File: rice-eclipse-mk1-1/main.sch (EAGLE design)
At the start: 197 parts, among them IC1 LMV321LICTRT, IC10 MCP6N11R, IC11 MCP6N11R, IC12 MCP6N11R, IC13 LMV321LICTRT, IC14 LMV321LICTRT, IC15 LMV321LICTRT, IC16 LMV321LICTRT, IC17 LMV321LICTRT, IC2 LMV321LICTRT, IC3 LMV321LICTRT, IC4 LMV321LICTRT, IC5 MCP6N11R, IC6 LMV321LICTRT, IC7 LMV321LICTRT, IC8 LMV321LICTRT, IC9 LMV321LICTRT, U6 1101M2S3CQE2

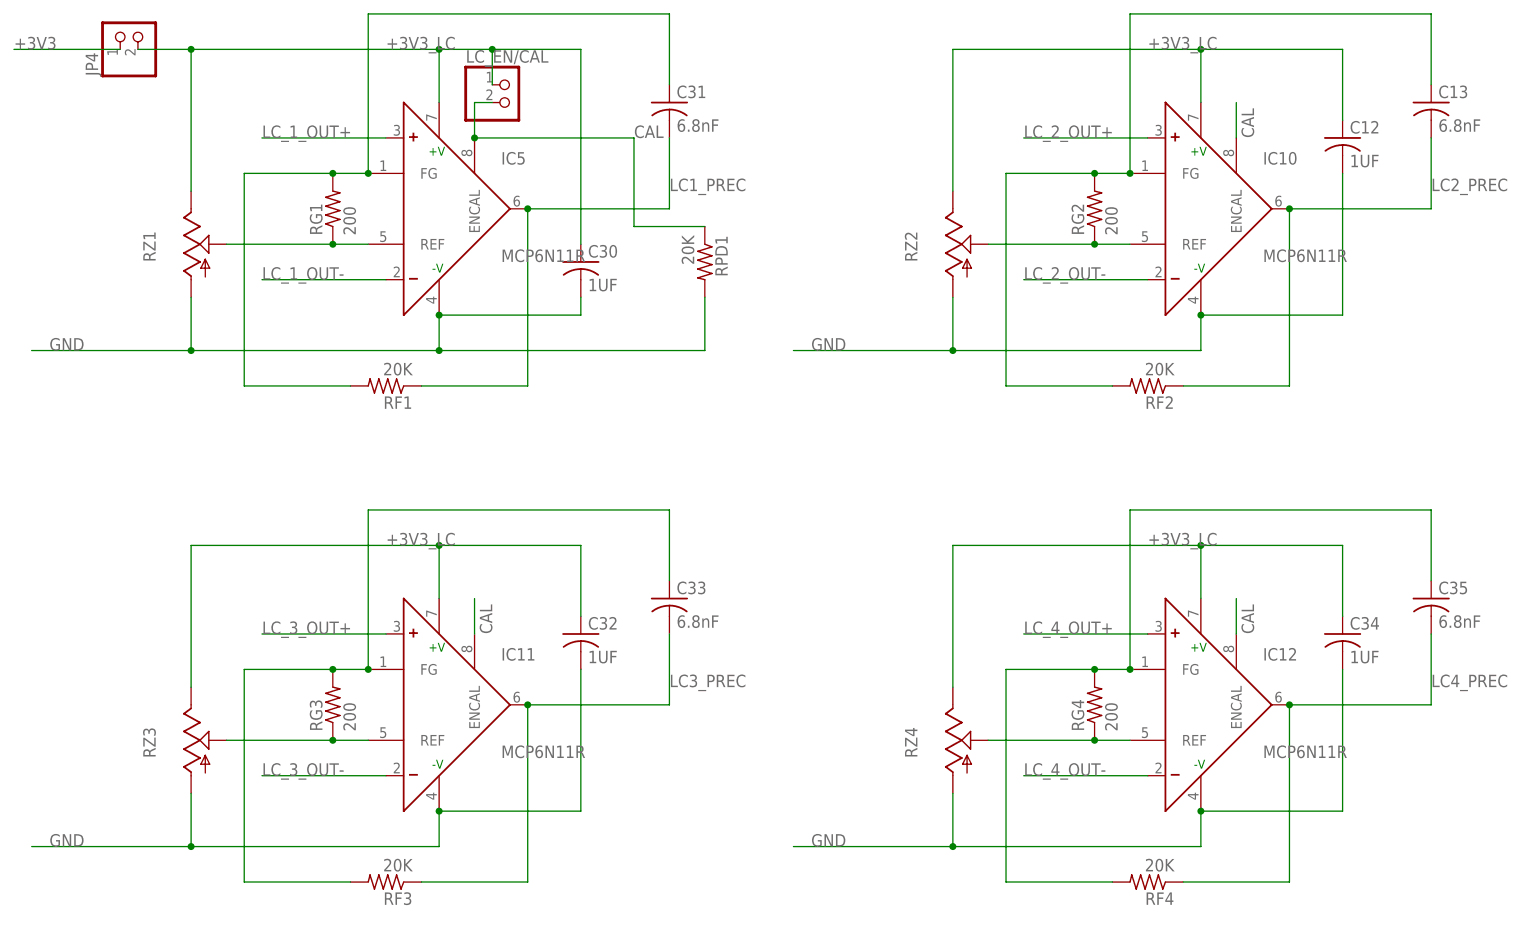
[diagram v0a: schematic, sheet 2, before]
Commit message: New schematics for Titan amp
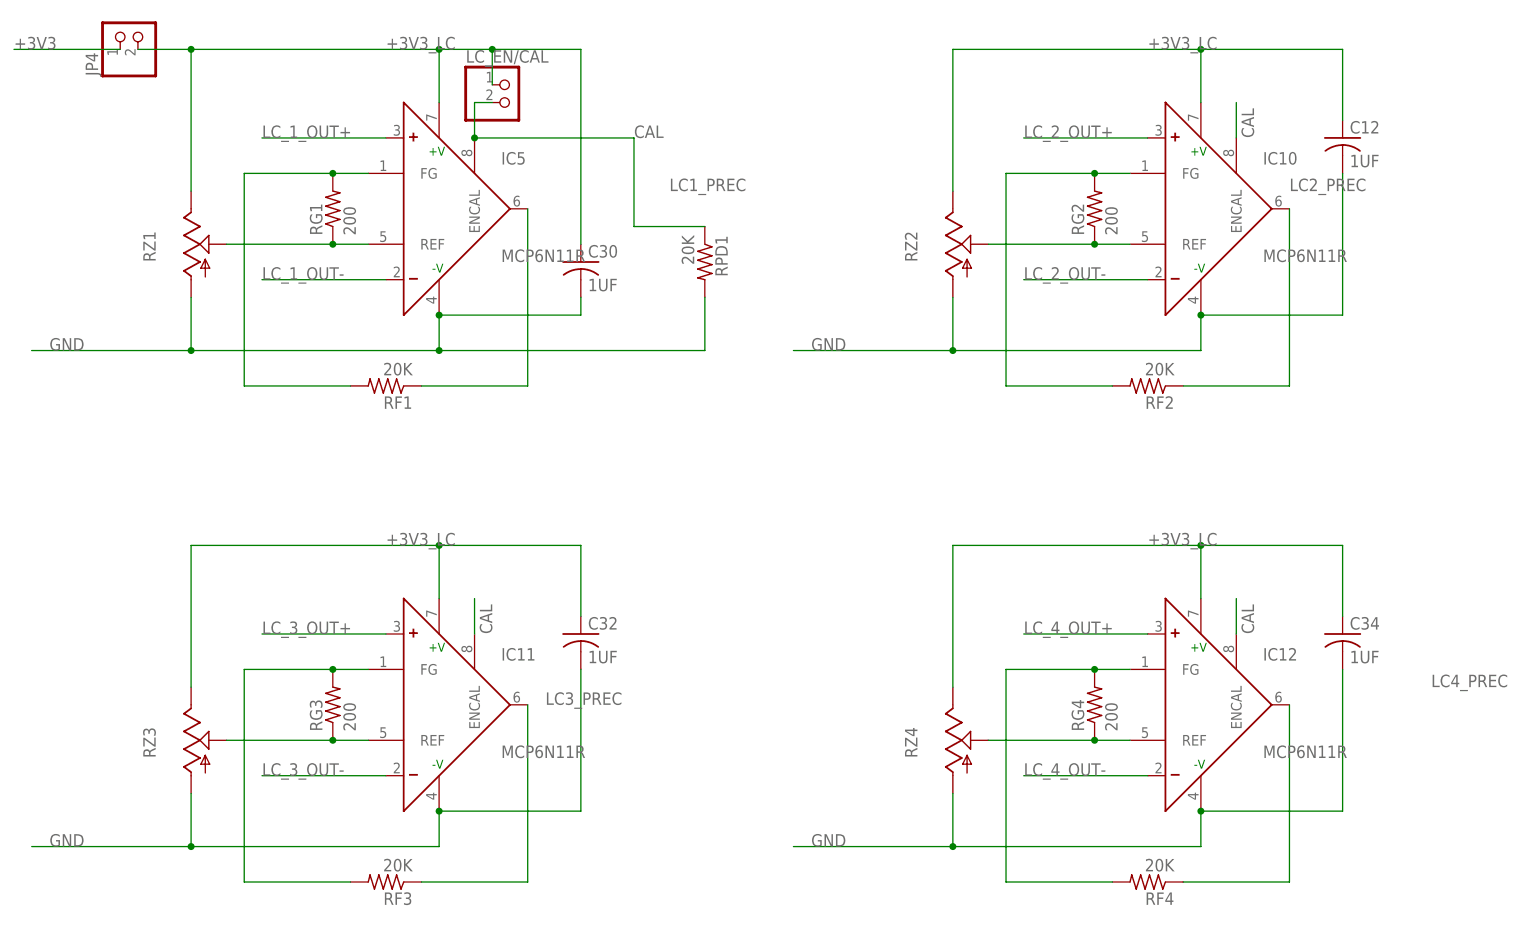
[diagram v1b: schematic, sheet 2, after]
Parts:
- removed C13, C31, C33, C35: 6.8nF, rcl:C-USC0805
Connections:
- net LC1_PREC: no longer C31.2
- net LC2_PREC: no longer C13.2
- net LC3_PREC: no longer C33.2
- net LC4_PREC: no longer C35.2
- net N$21: no longer C13.1
- net N$39: no longer C33.1
- net N$41: no longer C31.1
- net N$46: no longer C35.1
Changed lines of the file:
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@@
 <?xml version="1.0" encoding="utf-8"?>
 <!DOCTYPE eagle SYSTEM "eagle.dtd">
-<eagle version="8.7.1">
+<eagle version="8.7.0">
 <drawing>
 <settings>
-<setting alwaysvectorfont="yes"/>
+<setting alwaysvectorfont="no"/>
 <setting keepoldvectorfont="yes"/>
 <setting verticaltext="up"/>
@@
 <part name="C30" library="rcl" library_urn="urn:adsk.eagle:library:334" deviceset="C-US" device="C0805" package3d_urn="urn:adsk.eagle:package:23617/2" value="1UF"/>
 <part name="RZ1" library="pot" library_urn="urn:adsk.eagle:library:331" deviceset="TRIM_US-" device="S64W" package3d_urn="urn:adsk.eagle:package:22708/1"/>
-<part name="C31" library="rcl" library_urn="urn:adsk.eagle:library:334" deviceset="C-US" device="C0805" package3d_urn="urn:adsk.eagle:package:23617/2" value="6.8nF"/>
 <part name="JP4" library="pinhead" library_urn="urn:adsk.eagle:library:325" deviceset="PINHD-1X2" device="" package3d_urn="urn:adsk.eagle:package:22435/2"/>
 <part name="IC10" library="microchip-extra" deviceset="MCP6N11" device="R"/>
@@
 <part name="C12" library="rcl" library_urn="urn:adsk.eagle:library:334" deviceset="C-US" device="C0805" package3d_urn="urn:adsk.eagle:package:23617/2" value="1UF"/>
 <part name="RZ2" library="pot" library_urn="urn:adsk.eagle:library:331" deviceset="TRIM_US-" device="S64W" package3d_urn="urn:adsk.eagle:package:22708/1"/>
-<part name="C13" library="rcl" library_urn="urn:adsk.eagle:library:334" deviceset="C-US" device="C0805" package3d_urn="urn:adsk.eagle:package:23617/2" value="6.8nF"/>
 <part name="IC11" library="microchip-extra" deviceset="MCP6N11" device="R"/>
 <part name="RG3" library="rcl" library_urn="urn:adsk.eagle:library:334" deviceset="R-US_" device="R0805" value="200"/>
@@
 <part name="C32" library="rcl" library_urn="urn:adsk.eagle:library:334" deviceset="C-US" device="C0805" package3d_urn="urn:adsk.eagle:package:23617/2" value="1UF"/>
 <part name="RZ3" library="pot" library_urn="urn:adsk.eagle:library:331" deviceset="TRIM_US-" device="S64W" package3d_urn="urn:adsk.eagle:package:22708/1"/>
-<part name="C33" library="rcl" library_urn="urn:adsk.eagle:library:334" deviceset="C-US" device="C0805" package3d_urn="urn:adsk.eagle:package:23617/2" value="6.8nF"/>
 <part name="IC12" library="microchip-extra" deviceset="MCP6N11" device="R"/>
 <part name="RG4" library="rcl" library_urn="urn:adsk.eagle:library:334" deviceset="R-US_" device="R0805" value="200"/>
@@
 <part name="C34" library="rcl" library_urn="urn:adsk.eagle:library:334" deviceset="C-US" device="C0805" package3d_urn="urn:adsk.eagle:package:23617/2" value="1UF"/>
 <part name="RZ4" library="pot" library_urn="urn:adsk.eagle:library:331" deviceset="TRIM_US-" device="S64W" package3d_urn="urn:adsk.eagle:package:22708/1"/>
-<part name="C35" library="rcl" library_urn="urn:adsk.eagle:library:334" deviceset="C-US" device="C0805" package3d_urn="urn:adsk.eagle:package:23617/2" value="6.8nF"/>
 <part name="RPD1" library="rcl" library_urn="urn:adsk.eagle:library:334" deviceset="R-US_" device="R0805" value="20K"/>
 <part name="LC_EN/CAL" library="pinhead" library_urn="urn:adsk.eagle:library:325" deviceset="PINHD-1X2" device="" package3d_urn="urn:adsk.eagle:package:22435/2"/>
@@
 <instance part="C30" gate="G$1" x="96.52" y="129.54"/>
 <instance part="RZ1" gate="G$1" x="40.64" y="132.08"/>
-<instance part="C31" gate="G$1" x="109.22" y="152.4"/>
 <instance part="JP4" gate="G$1" x="33.02" y="162.56" rot="R90"/>
 <instance part="IC10" gate="G$1" x="185.42" y="137.16"/>
@@
 <instance part="C12" gate="G$1" x="205.74" y="147.32"/>
 <instance part="RZ2" gate="G$1" x="149.86" y="132.08"/>
-<instance part="C13" gate="G$1" x="218.44" y="152.4"/>
 <instance part="IC11" gate="G$1" x="76.2" y="66.04"/>
 <instance part="RG3" gate="G$1" x="60.96" y="66.04" rot="R90"/>
@@
 <instance part="C32" gate="G$1" x="96.52" y="76.2"/>
 <instance part="RZ3" gate="G$1" x="40.64" y="60.96"/>
-<instance part="C33" gate="G$1" x="109.22" y="81.28"/>
 <instance part="IC12" gate="G$1" x="185.42" y="66.04"/>
 <instance part="RG4" gate="G$1" x="170.18" y="66.04" rot="R90"/>
@@
 <instance part="C34" gate="G$1" x="205.74" y="76.2"/>
 <instance part="RZ4" gate="G$1" x="149.86" y="60.96"/>
-<instance part="C35" gate="G$1" x="218.44" y="81.28"/>
 <instance part="RPD1" gate="G$1" x="114.3" y="129.54" rot="R270"/>
 <instance part="LC_EN/CAL" gate="G$1" x="86.36" y="152.4"/>
@@
 <pinref part="RG1" gate="G$1" pin="2"/>
 <wire x1="60.96" y1="142.24" x2="66.04" y2="142.24" width="0.1524" layer="91"/>
-<pinref part="C31" gate="G$1" pin="1"/>
-<wire x1="109.22" y1="154.94" x2="109.22" y2="165.1" width="0.1524" layer="91"/>
-<wire x1="109.22" y1="165.1" x2="66.04" y2="165.1" width="0.1524" layer="91"/>
-<wire x1="66.04" y1="165.1" x2="66.04" y2="142.24" width="0.1524" layer="91"/>
-<junction x="66.04" y="142.24"/>
 <wire x1="60.96" y1="142.24" x2="48.26" y2="142.24" width="0.1524" layer="91"/>
 <junction x="60.96" y="142.24"/>
@@
 <pinref part="RG2" gate="G$1" pin="2"/>
 <wire x1="170.18" y1="142.24" x2="175.26" y2="142.24" width="0.1524" layer="91"/>
-<pinref part="C13" gate="G$1" pin="1"/>
-<wire x1="218.44" y1="154.94" x2="218.44" y2="165.1" width="0.1524" layer="91"/>
-<wire x1="218.44" y1="165.1" x2="175.26" y2="165.1" width="0.1524" layer="91"/>
-<wire x1="175.26" y1="165.1" x2="175.26" y2="142.24" width="0.1524" layer="91"/>
-<junction x="175.26" y="142.24"/>
 <wire x1="170.18" y1="142.24" x2="157.48" y2="142.24" width="0.1524" layer="91"/>
 <junction x="170.18" y="142.24"/>
@@
 <pinref part="RG3" gate="G$1" pin="2"/>
 <wire x1="60.96" y1="71.12" x2="66.04" y2="71.12" width="0.1524" layer="91"/>
-<pinref part="C33" gate="G$1" pin="1"/>
-<wire x1="109.22" y1="83.82" x2="109.22" y2="93.98" width="0.1524" layer="91"/>
-<wire x1="109.22" y1="93.98" x2="66.04" y2="93.98" width="0.1524" layer="91"/>
-<wire x1="66.04" y1="93.98" x2="66.04" y2="71.12" width="0.1524" layer="91"/>
-<junction x="66.04" y="71.12"/>
 <wire x1="60.96" y1="71.12" x2="48.26" y2="71.12" width="0.1524" layer="91"/>
 <junction x="60.96" y="71.12"/>
@@
 <pinref part="RG4" gate="G$1" pin="2"/>
 <wire x1="170.18" y1="71.12" x2="175.26" y2="71.12" width="0.1524" layer="91"/>
-<pinref part="C35" gate="G$1" pin="1"/>
-<wire x1="218.44" y1="83.82" x2="218.44" y2="93.98" width="0.1524" layer="91"/>
-<wire x1="218.44" y1="93.98" x2="175.26" y2="93.98" width="0.1524" layer="91"/>
-<wire x1="175.26" y1="93.98" x2="175.26" y2="71.12" width="0.1524" layer="91"/>
-<junction x="175.26" y="71.12"/>
 <wire x1="170.18" y1="71.12" x2="157.48" y2="71.12" width="0.1524" layer="91"/>
 <junction x="170.18" y="71.12"/>
@@
 <pinref part="IC5" gate="G$1" pin="OUT"/>
 <wire x1="88.9" y1="111.76" x2="88.9" y2="137.16" width="0.1524" layer="91"/>
-<pinref part="C31" gate="G$1" pin="2"/>
-<wire x1="88.9" y1="137.16" x2="109.22" y2="137.16" width="0.1524" layer="91"/>
-<wire x1="109.22" y1="137.16" x2="109.22" y2="147.32" width="0.1524" layer="91"/>
-<junction x="88.9" y="137.16"/>
 <pinref part="RF1" gate="G$1" pin="1"/>
 <wire x1="73.66" y1="111.76" x2="88.9" y2="111.76" width="0.1524" layer="91"/>
@@
 <pinref part="IC10" gate="G$1" pin="OUT"/>
 <wire x1="198.12" y1="111.76" x2="198.12" y2="137.16" width="0.1524" layer="91"/>
-<pinref part="C13" gate="G$1" pin="2"/>
-<wire x1="198.12" y1="137.16" x2="218.44" y2="137.16" width="0.1524" layer="91"/>
-<wire x1="218.44" y1="137.16" x2="218.44" y2="147.32" width="0.1524" layer="91"/>
-<junction x="198.12" y="137.16"/>
 <pinref part="RF2" gate="G$1" pin="1"/>
 <wire x1="182.88" y1="111.76" x2="198.12" y2="111.76" width="0.1524" layer="91"/>
-<label x="218.44" y="139.7" size="1.778" layer="95"/>
+<label x="198.12" y="139.7" size="1.778" layer="95"/>
 </segment>
 </net>
@@
 <pinref part="IC11" gate="G$1" pin="OUT"/>
 <wire x1="88.9" y1="40.64" x2="88.9" y2="66.04" width="0.1524" layer="91"/>
-<pinref part="C33" gate="G$1" pin="2"/>
-<wire x1="88.9" y1="66.04" x2="109.22" y2="66.04" width="0.1524" layer="91"/>
-<wire x1="109.22" y1="66.04" x2="109.22" y2="76.2" width="0.1524" layer="91"/>
-<junction x="88.9" y="66.04"/>
 <pinref part="RF3" gate="G$1" pin="1"/>
 <wire x1="73.66" y1="40.64" x2="88.9" y2="40.64" width="0.1524" layer="91"/>
-<label x="109.22" y="68.58" size="1.778" layer="95"/>
+<label x="91.44" y="66.04" size="1.778" layer="95"/>
 </segment>
 </net>
@@
 <pinref part="IC12" gate="G$1" pin="OUT"/>
 <wire x1="198.12" y1="40.64" x2="198.12" y2="66.04" width="0.1524" layer="91"/>
-<pinref part="C35" gate="G$1" pin="2"/>
-<wire x1="198.12" y1="66.04" x2="218.44" y2="66.04" width="0.1524" layer="91"/>
-<wire x1="218.44" y1="66.04" x2="218.44" y2="76.2" width="0.1524" layer="91"/>
-<junction x="198.12" y="66.04"/>
 <pinref part="RF4" gate="G$1" pin="1"/>
 <wire x1="182.88" y1="40.64" x2="198.12" y2="40.64" width="0.1524" layer="91"/>

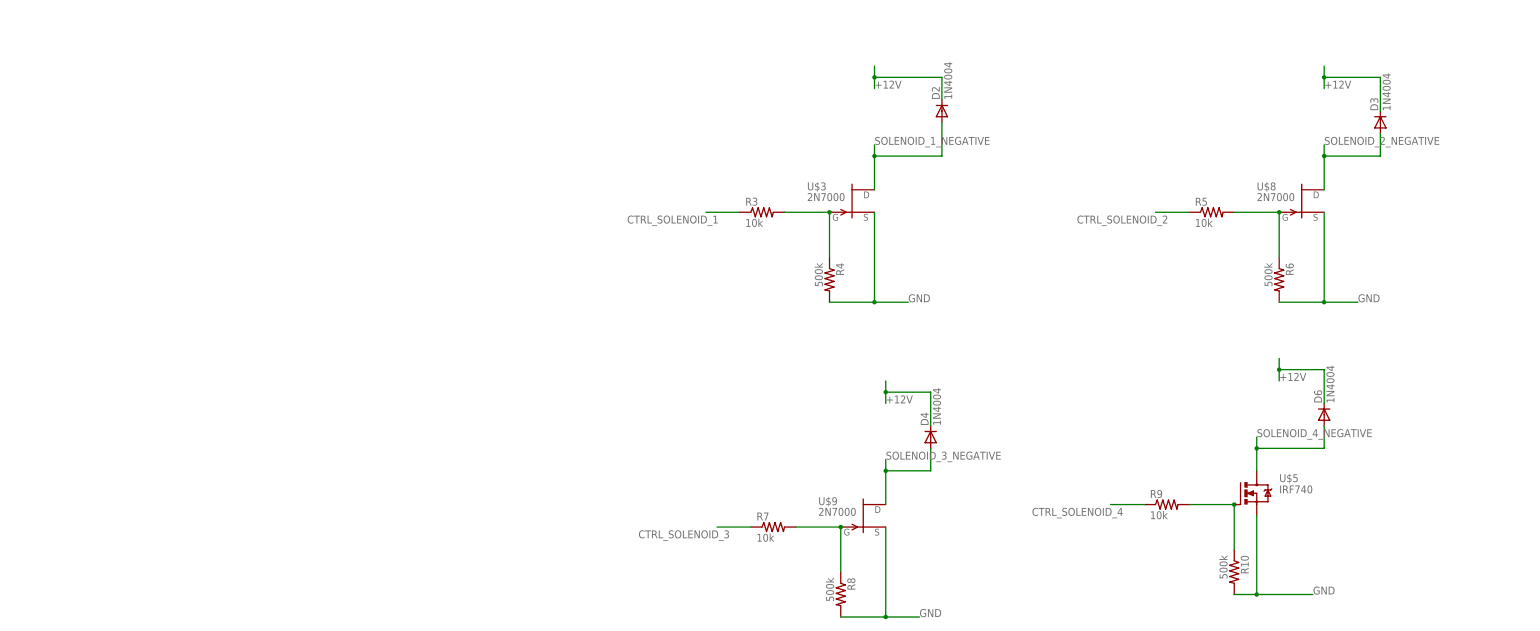
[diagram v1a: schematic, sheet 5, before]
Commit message: Make files match IRL
- Fix jumpers to take output of the op amp
directly, instead of across a resistor

- Changed adc inputs to 3.3V from 5V

- Added larger mosfets for TVC valves,
need to double check though.

Todo:
- Add igniter profiling circuitry

- Route the board
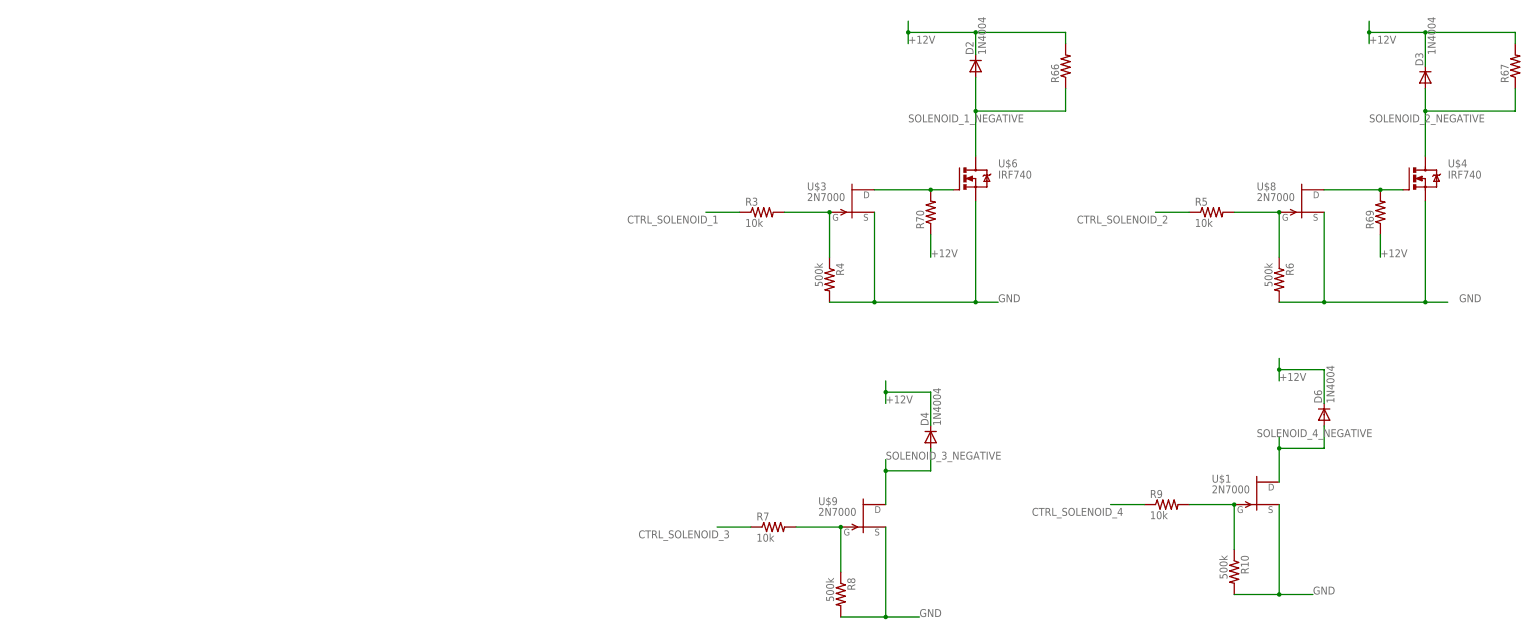
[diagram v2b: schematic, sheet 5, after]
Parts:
- removed U$5: IRF740, transistor-power:IRF740
- added R66, R67, R69, R70: (no value), rcl:R-US_R0805
- added U$1: 2N7000, transistor-fet-extra:2N7000
- added U$4, U$6: IRF740, transistor-power:IRF740
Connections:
- new net +3V3_LCAA: C10.1, IC13.+VS, LCAA_EN.2
- new net N$61: R70.2, U$3.D, U$6.G
- new net N$63: R69.2, U$4.G, U$8.D
- net +12V: now also R66.2, R67.2, R69.1, R70.1
- net +3V3: now also LCAA_EN.1
- net +5V: no longer LCAA_EN.1
- net +5V_LCAA: no longer C10.1, IC13.+VS, LCAA_EN.2
- net GND: now also U$1.S, U$4.S, U$6.S; no longer U$5.S
- net N$14: now also U$1.G; no longer U$5.G
- net N$18: now also LC1.2
- net N$20: now also LC2.2
- net N$23: no longer LC2.2
- net N$40: now also LC3.2
- net N$44: no longer LC3.2
- net N$49: now also LC4.2
- net N$50: no longer LC1.2
- net N$51: no longer LC4.2
- net N$58: now also LC5.2
- net N$59: no longer LC5.2
- net SOLENOID_1_NEGATIVE: now also R66.1, U$6.D; no longer U$3.D
- net SOLENOID_2_NEGATIVE: now also R67.1, U$4.D; no longer U$8.D
- net SOLENOID_4_NEGATIVE: now also U$1.D; no longer U$5.D
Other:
- moved on the sheet: D2, D3
